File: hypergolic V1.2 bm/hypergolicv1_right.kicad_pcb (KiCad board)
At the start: 2 copper layers, 119.9 x 87.7 mm, 25 parts, among them SW10 SW_Push, SW11 SW_Push, SW12 SW_Push, SW14 SW_Push, SW15 SW_Push, SW16 SW_Push, SW17 SW_Push, SW18 SW_Push, SW2 SW_Push, SW20 SW_Push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

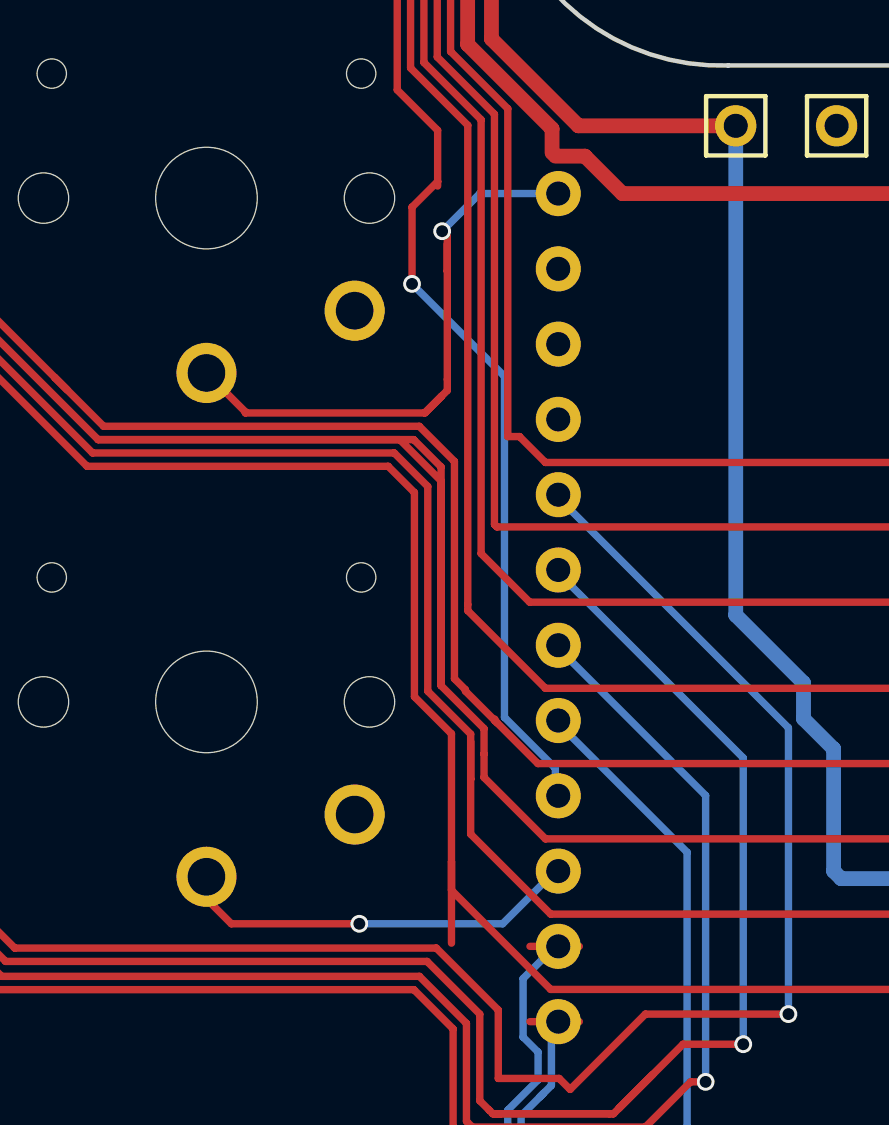
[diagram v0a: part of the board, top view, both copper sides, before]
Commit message: More trace corrections
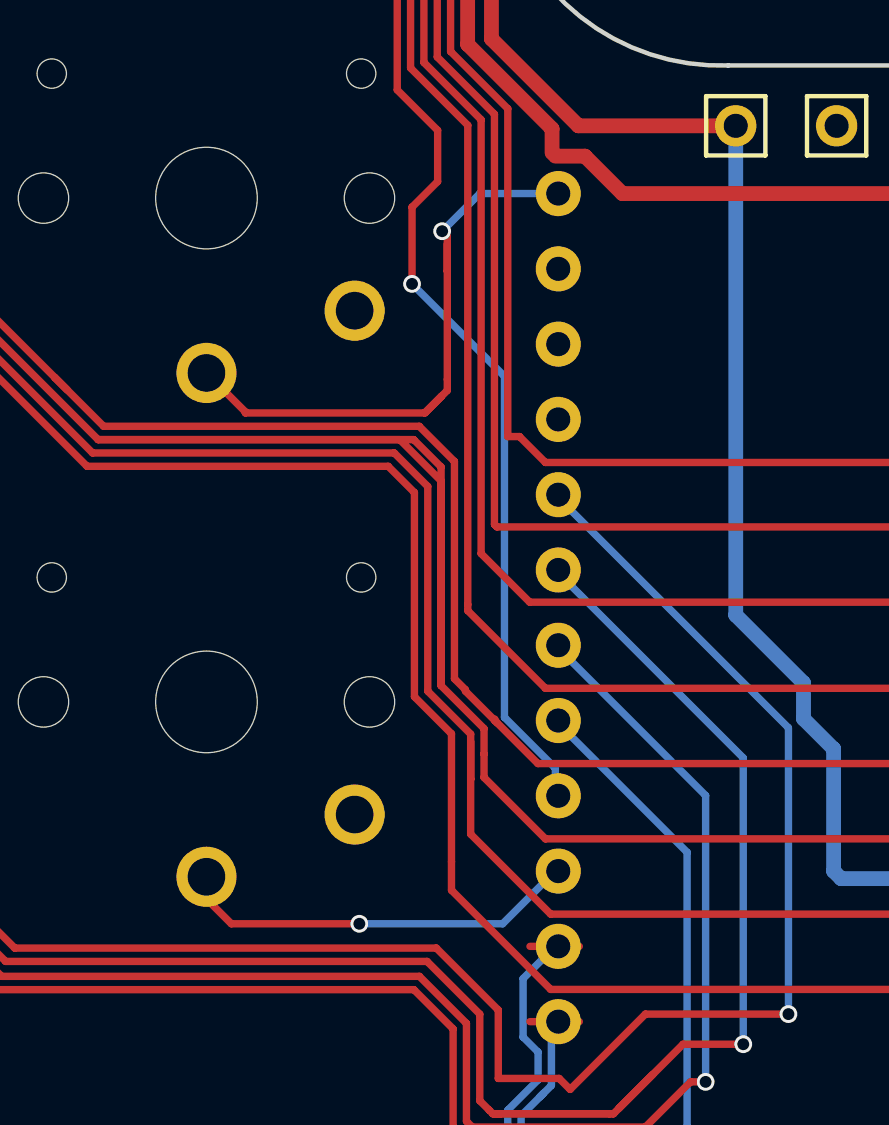
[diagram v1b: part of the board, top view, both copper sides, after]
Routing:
- net Switch9: track 65.1 -> 62.4 mm

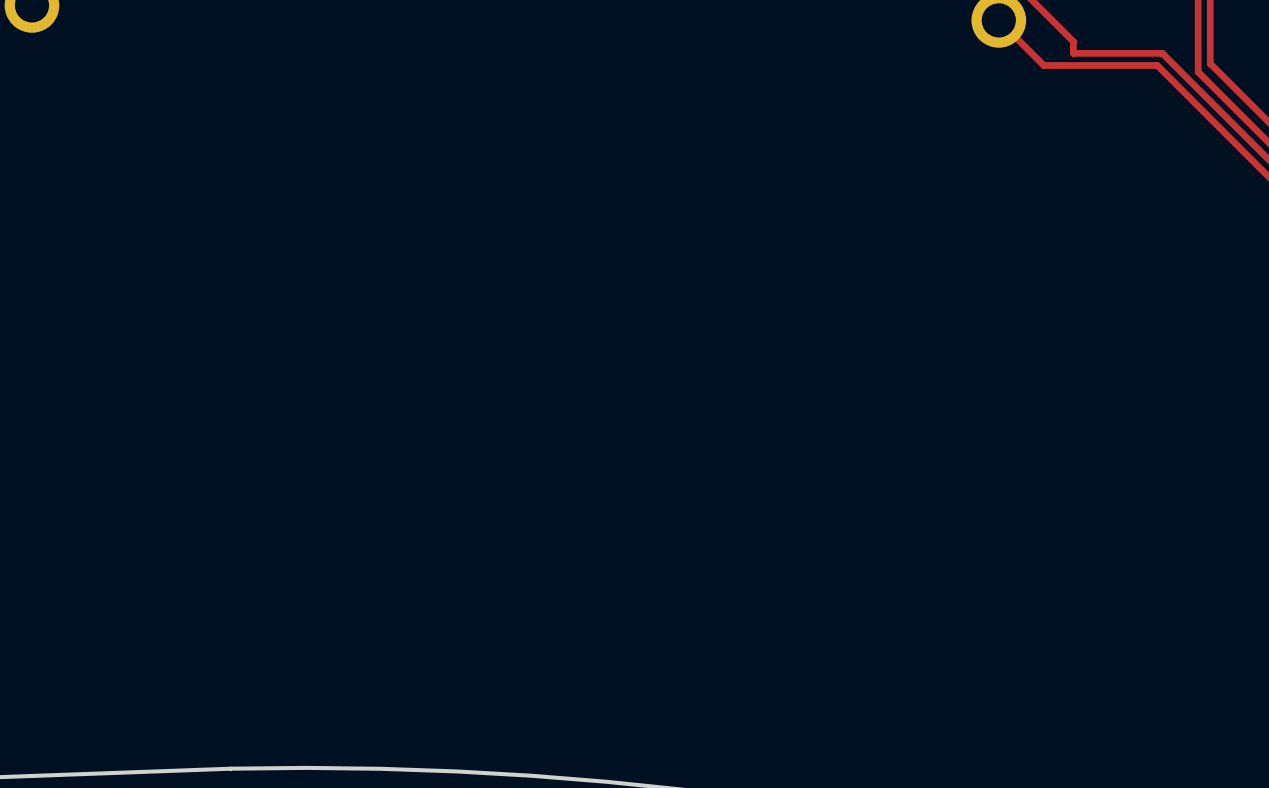
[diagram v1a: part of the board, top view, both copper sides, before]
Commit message: Add silkscreen to hypergolic
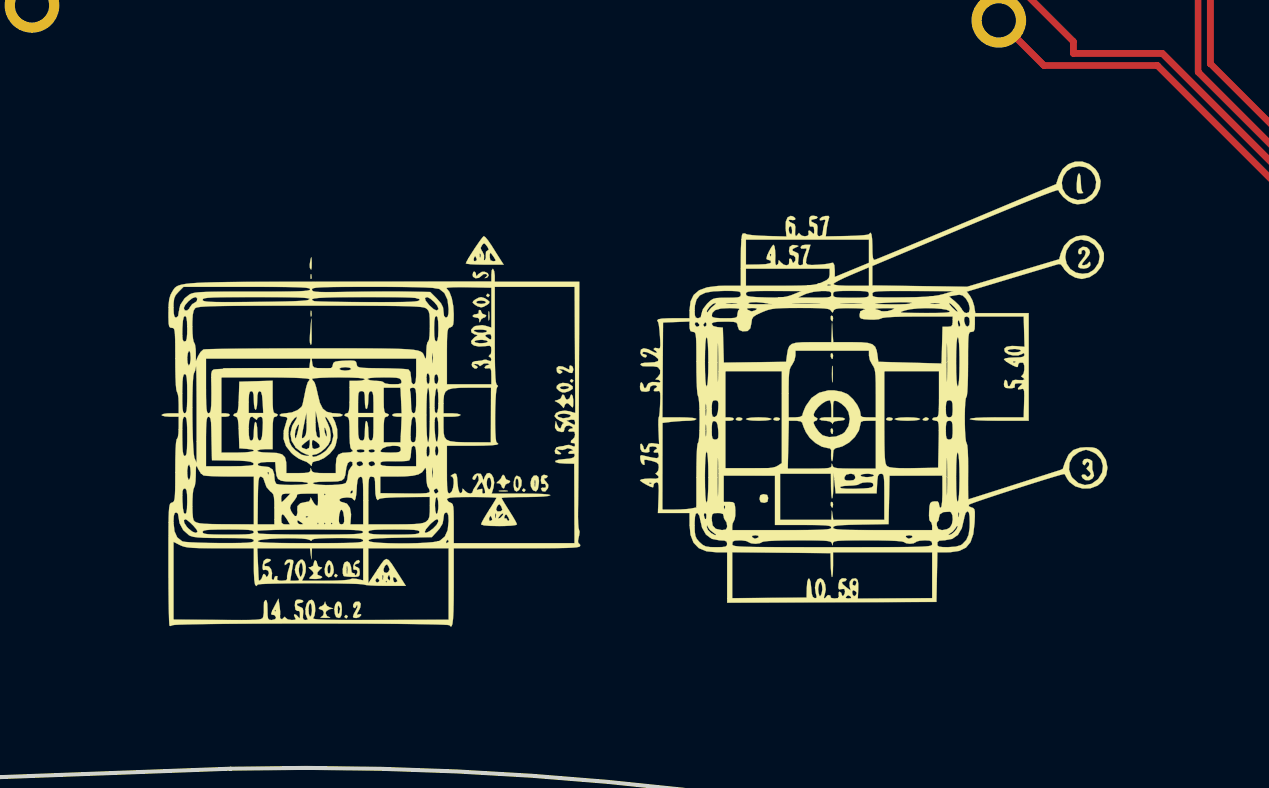
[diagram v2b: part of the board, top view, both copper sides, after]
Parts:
- added REF**: silk_pg2132_top, silkscreens:pg1232_top, F.Cu at (72.5, 83.9)
- added REF**: silk_pg1232_bottom, silkscreens:pg1232_bottom, F.Cu at (91.8, 83.9)

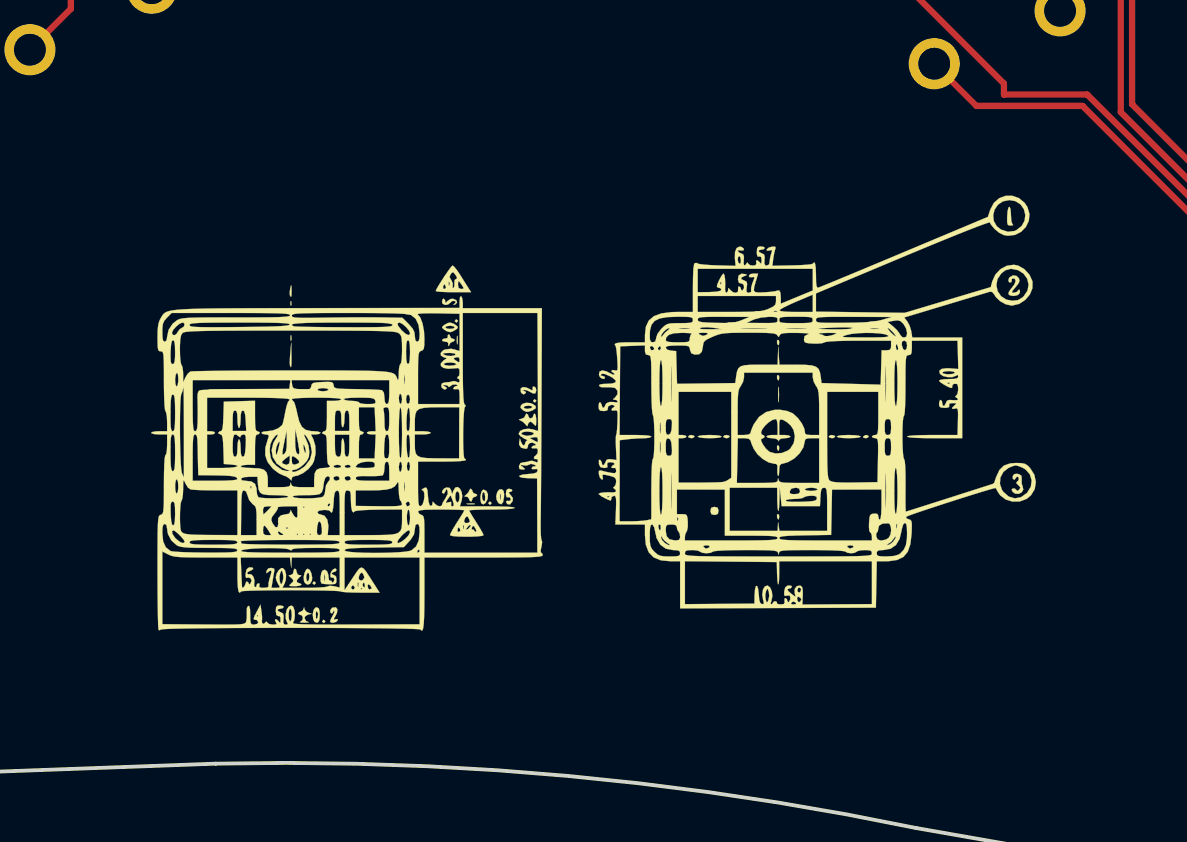
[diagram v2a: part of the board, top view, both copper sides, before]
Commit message: Swap silkscreen, add gerbers
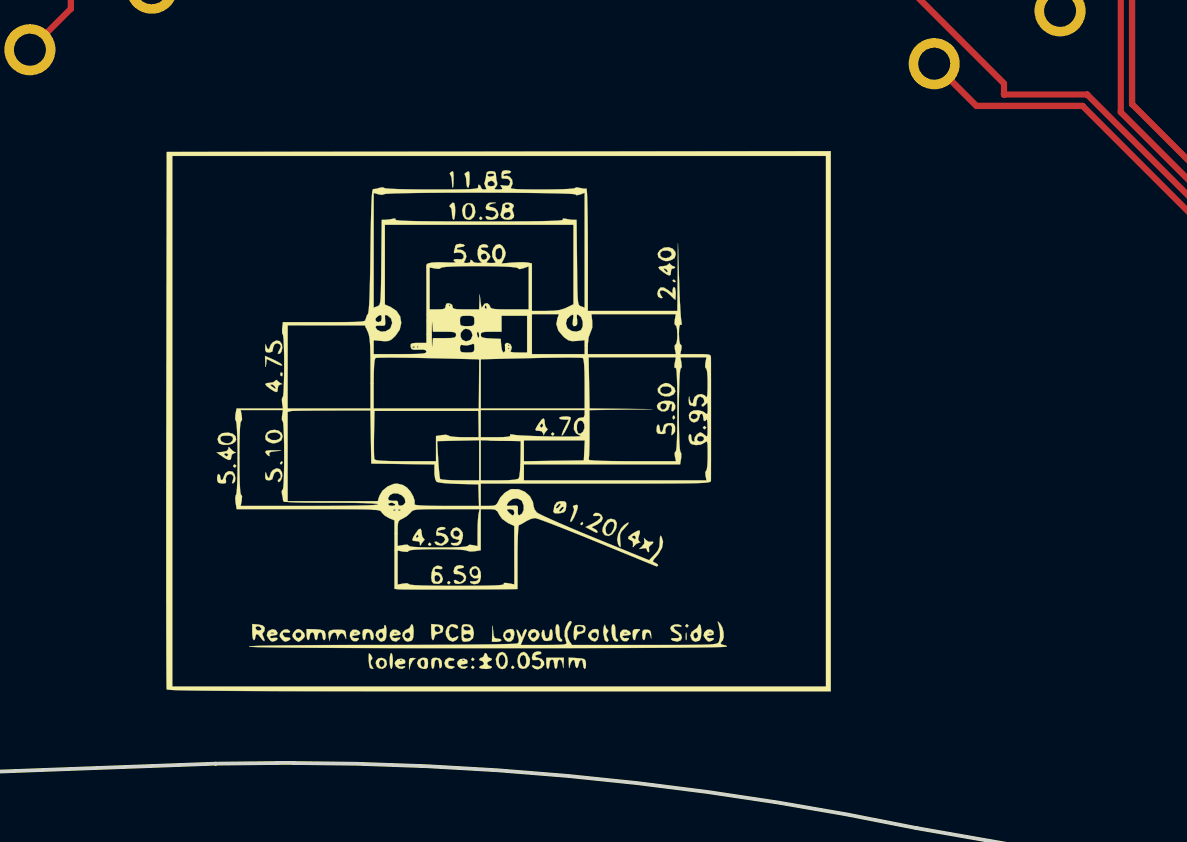
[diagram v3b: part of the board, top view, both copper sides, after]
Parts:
- removed the REF** at (72.5, 83.9)
- removed the REF** at (91.8, 83.9)
- added REF**: silk_pg1232_footprint, silkscreens:pg1232_footprint, F.Cu at (80.0, 82.8)
